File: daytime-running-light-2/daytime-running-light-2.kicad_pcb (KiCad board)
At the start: 2 copper layers, 57.8 x 87.8 mm, 58 parts, among them J1 Conn_01x01_Socket, J2 Conn_01x01_Socket, J3 Conn_01x01_Socket, J4 Conn_01x01_Socket, J5 Conn_01x01_Socket, J6 Conn_01x01_Pin, J7 Conn_01x01_Socket, J8 Conn_01x01_Socket, J9 Conn_01x01_Socket, Q1 BC548, Q2 IRF9540N, Q3 IRFB3004PbF, SW1 SW_SPST, U1 L7812, U2 TLC555xP, U3 L7812, U4 4001, U5 4069, U6 IRS10752LPbF

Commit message: [DRL] Fix and update PCB and schematic  Use BAT2 and VCC2  Add missing net on PCB  Improve zones for BAT2 and GND2
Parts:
- moved J8 6.65 mm to (61.0, 102.9)
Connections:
- net +12V renamed +BATT2
- net /VCC_STAB2 renamed VCC2
- C4 pad 1: /VCC_STAB -> VCC
- C8 pad 1: /VCC_STAB -> VCC
- C9 pad 1: /VCC_STAB -> VCC
- J1 pad 1: VCC -> +BATT
- R4 pad 2: /VCC_STAB -> VCC
- SW1 pad 1: VCC -> +BATT
- U1 pad 3: /VCC_STAB -> VCC
- U4 pad 14: /VCC_STAB -> VCC
- U5 pad 14: /VCC_STAB -> VCC
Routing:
- net GND2: track 129.0 -> 92.9 mm
- net /VCC_STAB: track 30.0 -> 0.00 mm
- net VCC: track 5.27 -> 30.0 mm
- net +BATT: track 0.00 -> 5.27 mm
- net /HEADLIGHT: track 1.80 -> 6.36 mm
- added copper zone on B.Cu, net VCC
- removed copper zone on B.Cu, net /VCC_STAB

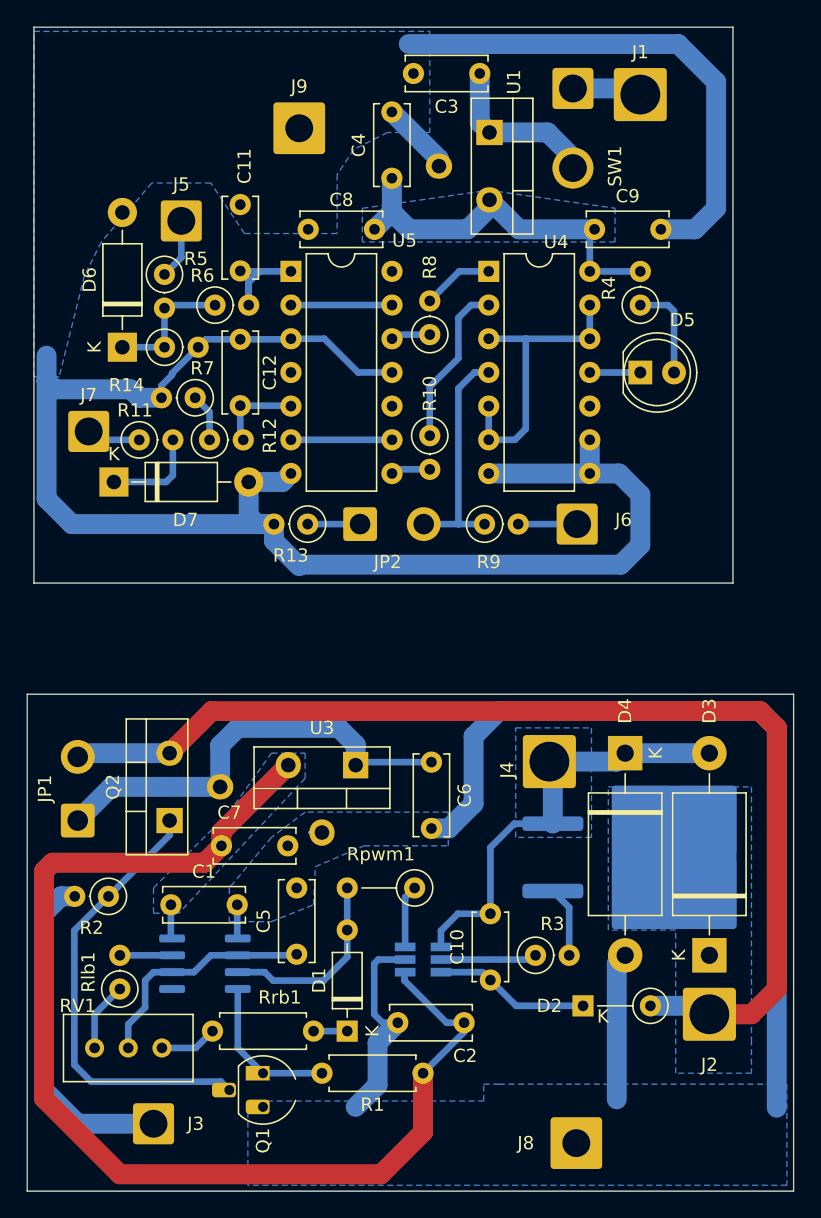
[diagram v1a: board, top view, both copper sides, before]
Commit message: [DRL] Improve schematic and PCB
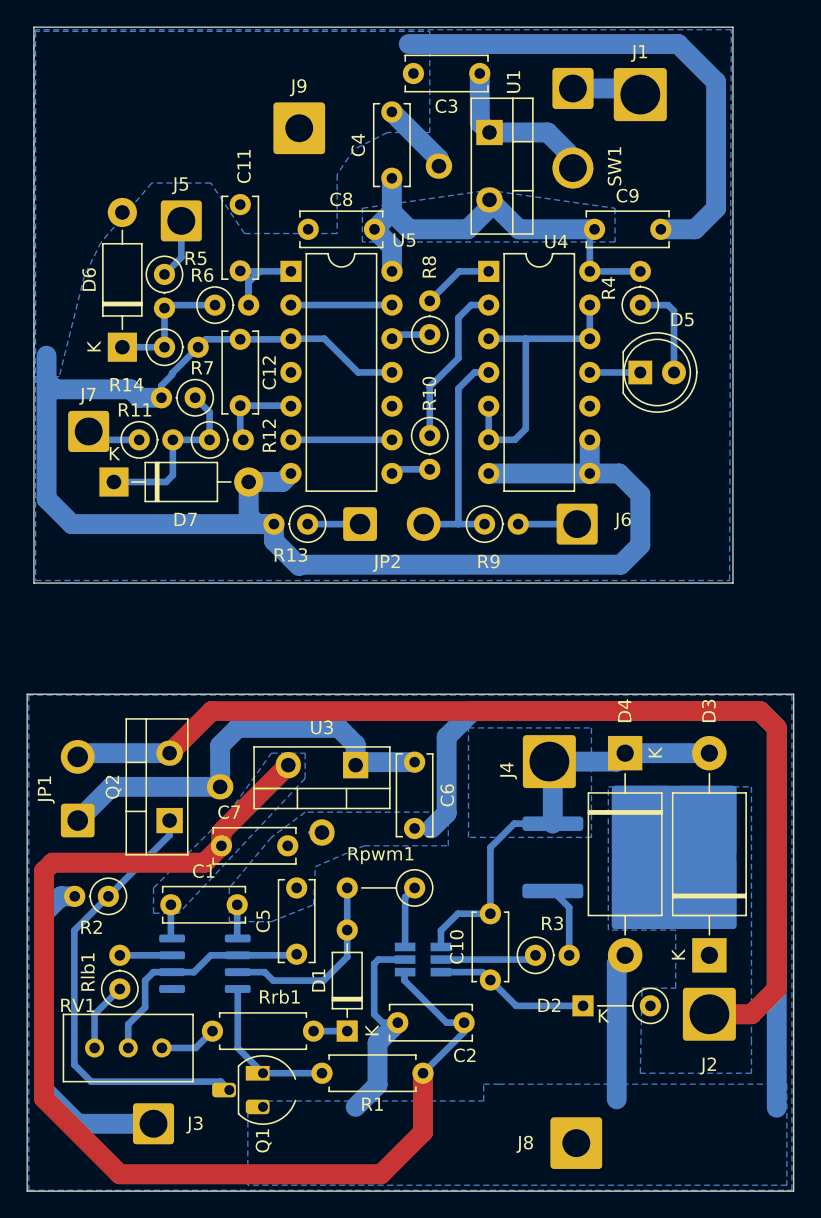
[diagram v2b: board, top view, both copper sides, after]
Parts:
- D3, D4: value 1.5KExxA -> 1.5KE18A
- moved C6 1.27 mm to (48.8, 74.1)
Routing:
- net +BATT2: track 85.2 -> 81.4 mm
- net VCC: track 30.0 -> 33.7 mm
- net Net-(D7-K): track 10.9 -> 13.7 mm
- net Net-(JP1-A): track 33.9 -> 32.3 mm
- added copper zone on B.Cu, net (none)
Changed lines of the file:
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@@
         (effects (font (size 1 1) (thickness 0.15)))
     )
-    (fp_text value "1.5KExxA" (at 7.62 3.77 90) (layer "F.Fab")
+    (fp_text value "1.5KE18A" (at 7.62 3.77 90) (layer "F.Fab")
         (effects (font (size 1 1) (thickness 0.15)))
     )
@@
   )
   (footprint "Capacitor_THT:C_Disc_D6.0mm_W2.5mm_P5.00mm" (layer "F.Cu")
-    (at 50.038 74.1445 -90)
+    (at 48.768 74.1445 -90)
     (descr "C, Disc series, Radial, pin pitch=5.00mm, , diameter*width=6*2.5mm^2, Capacitor, http://cdn-reichelt.de/documents/datenblatt/B300/DS_KERKO_TC.pdf")
     (tags "C Disc series Radial pin pitch 5.00mm  diameter 6mm width 2.5mm Capacitor")
@@
         (effects (font (size 1 1) (thickness 0.15)))
     )
-    (fp_text value "1.5KExxA" (at 7.62 3.77 90) (layer "F.Fab")
+    (fp_text value "1.5KE18A" (at 7.62 3.77 90) (layer "F.Fab")
         (effects (font (size 1 1) (thickness 0.15)))
     )
@@
   (segment (start 48.053 89.9795) (end 48.006 90.0265) (width 0.5) (layer "B.Cu") (net 1))
   (segment (start 48.006 90.6145) (end 51.181 93.7895) (width 0.5) (layer "B.Cu") (net 1))
+  (segment (start 51.181 78.0015) (end 50.038 79.1445) (width 1.5) (layer "B.Cu") (net 2))
   (segment (start 47.498 93.7895) (end 45.974 95.3135) (width 1.5) (layer "B.Cu") (net 2))
   (segment (start 35.393 87.3995) (end 35.433 87.4395) (width 0.5) (layer "B.Cu") (net 2))
+  (segment (start 74.803 70.2945) (end 53.1495 70.2945) (width 1.5) (layer "B.Cu") (net 2))
+  (segment (start 76.073 100.203) (end 76.073 71.5645) (width 1.5) (layer "B.Cu") (net 2))
+  (segment (start 76.073 71.5645) (end 74.803 70.2945) (width 1.5) (layer "B.Cu") (net 2))
   (segment (start 64.008 89.3445) (end 64.643 88.7095) (width 1.5) (layer "B.Cu") (net 2))
   (segment (start 45.72 89.3445) (end 46.035 89.0295) (width 0.5) (layer "B.Cu") (net 2))
-  (segment (start 53.213 72.1995) (end 55.118 70.2945) (width 1.5) (layer "B.Cu") (net 2))
+  (segment (start 53.1495 70.2945) (end 51.181 72.263) (width 1.5) (layer "B.Cu") (net 2))
   (segment (start 47.498 93.7895) (end 46.355 93.7895) (width 0.5) (layer "B.Cu") (net 2))
   (segment (start 41.783 79.452) (end 40.8405 79.452) (width 0.25) (layer "B.Cu") (net 2))
+  (segment (start 51.181 72.263) (end 51.181 78.0015) (width 1.5) (layer "B.Cu") (net 2))
   (segment (start 45.974 95.3135) (end 45.974 98.4885) (width 1.5) (layer "B.Cu") (net 2))
   (segment (start 64.008 99.568) (end 64.008 89.3445) (width 1.5) (layer "B.Cu") (net 2))
-  (segment (start 76.073 71.5645) (end 76.073 100.203) (width 1.5) (layer "B.Cu") (net 2))
-  (segment (start 53.213 77.2795) (end 53.213 72.1995) (width 1.5) (layer "B.Cu") (net 2))
   (segment (start 46.355 93.7895) (end 45.72 93.1545) (width 0.5) (layer "B.Cu") (net 2))
   (segment (start 35.393 84.8995) (end 35.393 87.3995) (width 0.5) (layer "B.Cu") (net 2))
   (segment (start 46.035 89.0295) (end 48.053 89.0295) (width 0.5) (layer "B.Cu") (net 2))
-  (segment (start 50.038 79.1445) (end 51.348 79.1445) (width 1.5) (layer "B.Cu") (net 2))
-  (segment (start 74.803 70.2945) (end 76.073 71.5645) (width 1.5) (layer "B.Cu") (net 2))
   (segment (start 49.7305 79.452) (end 50.038 79.1445) (width 0.25) (layer "B.Cu") (net 2))
   (segment (start 45.72 93.1545) (end 45.72 89.3445) (width 0.5) (layer "B.Cu") (net 2))
-  (segment (start 51.348 79.1445) (end 53.213 77.2795) (width 1.5) (layer "B.Cu") (net 2))
-  (segment (start 55.118 70.2945) (end 74.803 70.2945) (width 1.5) (layer "B.Cu") (net 2))
   (segment (start 45.974 98.4885) (end 44.323 100.1395) (width 1.5) (layer "B.Cu") (net 2))
   (segment (start 54.356 52.3825) (end 61.976 52.3825) (width 1.5) (layer "B.Cu") (net 3))
@@
   (segment (start 23.648 73.4695) (end 23.368 73.7495) (width 1.5) (layer "B.Cu") (net 4))
   (segment (start 30.2955 73.4695) (end 23.648 73.4695) (width 1.5) (layer "B.Cu") (net 4))
-  (segment (start 66.548001 92.5195) (end 70.358 92.5195) (width 1.5) (layer "B.Cu") (net 4))
   (segment (start 28.448 92.6465) (end 28.448 90.6145) (width 0.5) (layer "B.Cu") (net 5))
   (segment (start 27.178 95.6945) (end 27.178 93.9165) (width 0.5) (layer "B.Cu") (net 5))
@@
   (segment (start 30.483 89.9795) (end 32.131 89.9795) (width 0.5) (layer "B.Cu") (net 5))
   (segment (start 39.798 88.7095) (end 39.878 88.6295) (width 0.5) (layer "B.Cu") (net 5))
-  (segment (start 49.8105 74.372) (end 50.038 74.1445) (width 0.25) (layer "B.Cu") (net 6))
   (segment (start 44.323 72.8345) (end 44.323 74.372) (width 1.5) (layer "B.Cu") (net 6))
+  (segment (start 48.768 74.1445) (end 44.5505 74.1445) (width 1.5) (layer "B.Cu") (net 6))
   (segment (start 34.1055 76.0095) (end 34.1055 72.892) (width 1.5) (layer "B.Cu") (net 6))
+  (segment (start 44.5505 74.1445) (end 44.323 74.372) (width 1.5) (layer "B.Cu") (net 6))
   (segment (start 35.433 71.5645) (end 43.053 71.5645) (width 1.5) (layer "B.Cu") (net 6))
-  (segment (start 50.038 74.1445) (end 44.5505 74.1445) (width 0.5) (layer "B.Cu") (net 6))
   (segment (start 25.908 76.0095) (end 23.368 78.5495) (width 1.5) (layer "B.Cu") (net 6))
   (segment (start 34.1055 72.892) (end 35.433 71.5645) (width 1.5) (layer "B.Cu") (net 6))
   (segment (start 34.1055 76.0095) (end 25.908 76.0095) (width 1.5) (layer "B.Cu") (net 6))
-  (segment (start 44.5505 74.1445) (end 44.323 74.372) (width 0.5) (layer "B.Cu") (net 6))
   (segment (start 43.053 71.5645) (end 44.323 72.8345) (width 1.5) (layer "B.Cu") (net 6))
   (segment (start 39.4435 37.1425) (end 37.084 37.1425) (width 0.5) (layer "B.Cu") (net 7))
@@
   (segment (start 30.5435 49.8475) (end 30.5435 52.5145) (width 0.5) (layer "B.Cu") (net 14))
   (segment (start 30.5435 52.5145) (end 30.0355 53.0225) (width 0.5) (layer "B.Cu") (net 14))
+  (segment (start 30.5435 49.8475) (end 33.308499 49.8475) (width 0.5) (layer "B.Cu") (net 14))
   (segment (start 60.706 23.3525) (end 65.326 23.3525) (width 1.5) (layer "B.Cu") (net 15))
   (segment (start 65.326 23.3525) (end 65.786 23.8125) (width 1.5) (layer "B.Cu") (net 15))
@@
   (segment (start 62.3335 33.9725) (end 56.636 33.9725) (width 1.5) (layer "B.Cu") (net 16))
   (segment (start 48.3635 33.9725) (end 52.7685 33.9725) (width 1.5) (layer "B.Cu") (net 16))
+  (segment (start 47.0635 37.1425) (end 47.0635 35.2925) (width 1.5) (layer "B.Cu") (net 16))
   (segment (start 47.0535 30.1225) (end 47.0535 32.6625) (width 1.5) (layer "B.Cu") (net 16))
   (segment (start 61.976 37.1425) (end 61.976 34.33) (width 0.5) (layer "B.Cu") (net 16))
@@
   (segment (start 61.981 37.1475) (end 61.976 37.1425) (width 0.5) (layer "B.Cu") (net 16))
   (segment (start 54.4135 32.3275) (end 54.4135 31.75) (width 1.5) (layer "B.Cu") (net 16))
+  (segment (start 47.0635 35.2925) (end 45.7435 33.9725) (width 1.5) (layer "B.Cu") (net 16))
   (segment (start 52.7685 33.9725) (end 54.4135 32.3275) (width 1.5) (layer "B.Cu") (net 16))
   (segment (start 62.3335 36.785) (end 61.976 37.1425) (width 0.25) (layer "B.Cu") (net 16))
@@
         (xy 74.168 95.0595)
         (xy 74.168 97.5995)
-        (xy 68.453 97.5995)
+        (xy 65.786 97.5995)
+        (xy 65.913 91.186)
+        (xy 68.453 91.186)
         (xy 68.453 86.8045)
         (xy 63.373 86.8045)
@@
     (polygon
       (pts
-        (xy 56.388 79.8195)
-        (xy 56.388 71.5645)
+        (xy 52.832 79.8195)
+        (xy 52.832 71.5645)
         (xy 62.103 71.5645)
         (xy 62.103 79.8195)
@@
     )
   )
+  (zone (net 0) (net_name "") (layer "B.Cu") (hatch edge 0.5)
+    (connect_pads yes (clearance 0.75))
+    (min_thickness 0.75) (filled_areas_thickness no)
+    (fill yes (thermal_gap 0.5) (thermal_bridge_width 1) (island_removal_mode 1) (island_area_min 10))
+    (polygon
+      (pts
+        (xy 20.193 19.05)
+        (xy 20.193 60.452)
+        (xy 72.517 60.452)
+        (xy 72.644 18.923)
+        (xy 20.193 18.923)
+      )
+    )
+  )
   (zone (net 2) (net_name "GND2") (layer "B.Cu") (hatch edge 0.5)
+    (priority 1)
     (connect_pads yes (clearance 0.5))
     (min_thickness 0.25) (filled_areas_thickness no)
@@
       )
     )
+  )
+  (zone (net 0) (net_name "") (layer "B.Cu") (hatch edge 0.5)
+    (connect_pads yes (clearance 0.75))
+    (min_thickness 0.75) (filled_areas_thickness no)
+    (fill yes (thermal_gap 0.5) (thermal_bridge_width 1) (island_removal_mode 1) (island_area_min 10))
+    (polygon
+      (pts
+        (xy 19.685 106.426)
+        (xy 77.216 106.426)
+        (xy 77.216 69.088)
+        (xy 19.685 69.088)
+      )
+    )
